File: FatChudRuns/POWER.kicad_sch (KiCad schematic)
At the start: 0 parts

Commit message: add usb c power circuitry, added led for power indication, increased resistance of ethernet leds light to 220ohms
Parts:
- added C21, C22, C23, C24: 1uF, symbol Device:C_Polarized_US
- added D1, D2: LED, symbol Device:LED
- added J4: USB_C_Receptacle_USB2.0_16P, symbol Connector:USB_C_Receptacle_USB2.0_16P
- added R47, R48: 5.1k, Resistor_SMD:R_0603_1608Metric, symbol Device:R
- added R49: 4.7k, Resistor_SMD:R_0603_1608Metric, symbol Device:R
- added R50, R51: 220, Resistor_SMD:R_0603_1608Metric, symbol Device:R
- added SW3: SW_DIP_x01, symbol Switch:SW_DIP_x01
- added U3: USBLC6-2SC6, Package_TO_SOT_SMD:SOT-23-6, symbol Power_Protection:USBLC6-2SC6
- added U5, U6: ST730M33R, SOT_30M33R_STM:SOT_30M33R_STM, symbol ST730:ST730M33R
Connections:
- new net: D2.2 (A), R51.2
- new net: D1.2 (A), R50.2
- new net: J4.A5 (CC1), R48.1
- new net: J4.A6 (D+), J4.B6 (D+), U3.3 (I/O2)
- new net: J4.A7 (D-), J4.B7 (D-), U3.1 (I/O1)
- new net: J4.B5 (CC2), R47.1
- new net +3.3V: C22.1, R51.1, U6.1 (VOUT)
- new net +3.3VA: C24.1, R50.1, U5.1 (VOUT)
- new net +5V: C21.1, C23.1, J4.A4 (VBUS), J4.A9 (VBUS), J4.B4 (VBUS), J4.B9 (VBUS), R49.1, U3.5 (VBUS), U5.3 (VIN), U6.3 (VIN)
- new net GND: C21.2, C22.2, C23.2, C24.2, D1.1 (K), D2.1 (K), J4.A1 (GND), J4.A12 (GND), J4.B1 (GND), J4.B12 (GND), J4.S1 (SHIELD), R47.2, R48.2, SW3.1, U3.2 (GND), U5.2 (GND), U6.2 (GND)
- new net LDO_EN: R49.2, SW3.2, U5.5 (EN), U6.5 (EN)
- new net USB_D+: U3.4 (I/O2)
- new net USB_D-: U3.6 (I/O1)
- no-connect marks 0 -> 4

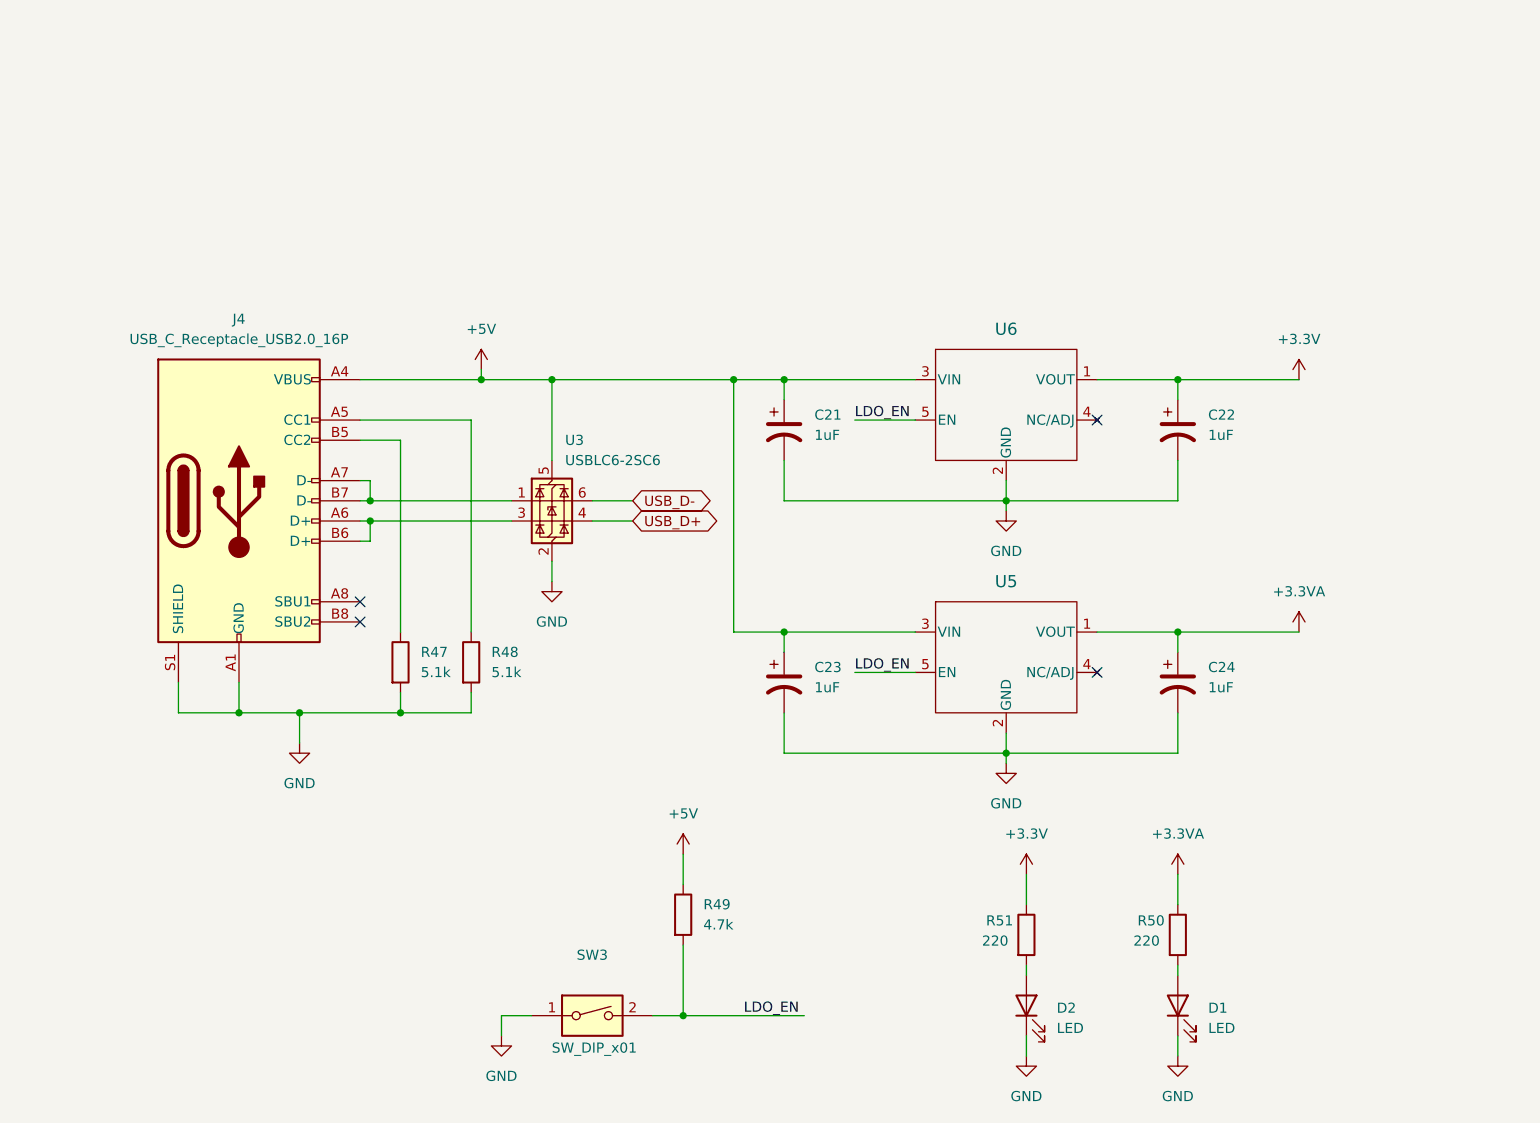
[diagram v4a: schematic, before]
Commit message: sorted out erc errors and warning, connected tvs diodes to jtag
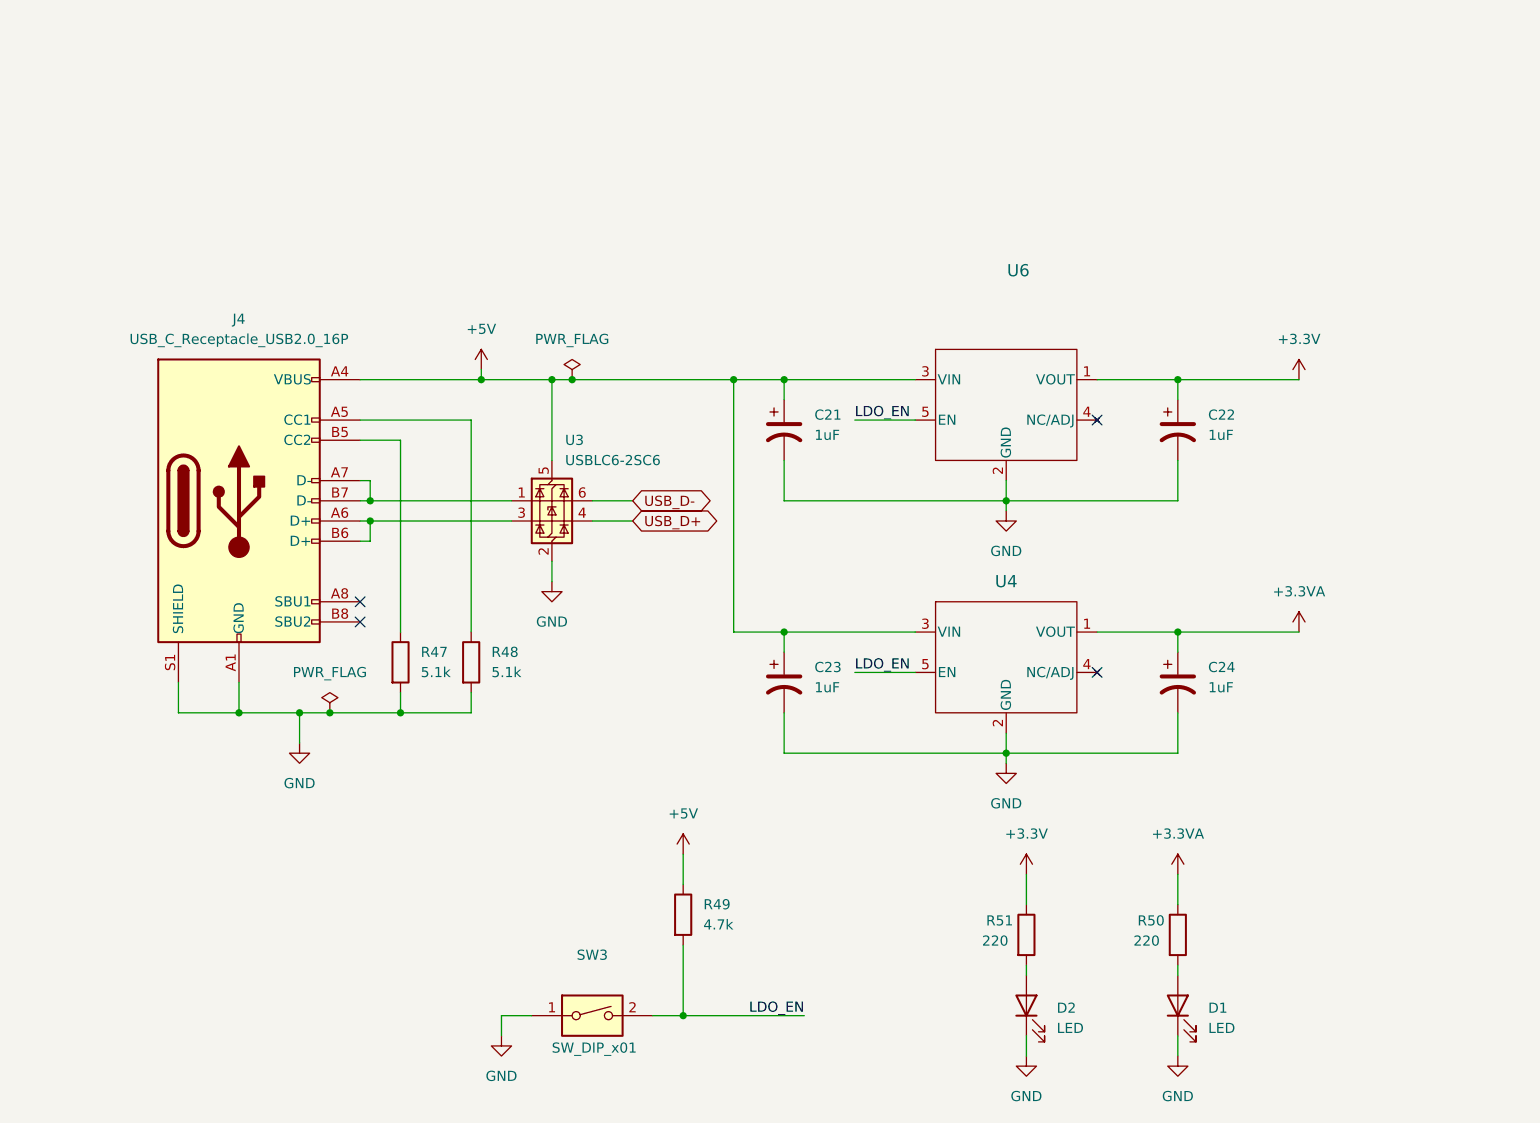
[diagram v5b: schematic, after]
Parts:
- removed U5: ST730M33R, SOT_30M33R_STM:SOT_30M33R_STM, symbol ST730:ST730M33R
- added U4: ST730M33R, SOT_30M33R_STM:SOT_30M33R_STM, symbol ST730:ST730M33R
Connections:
- net +3.3VA: now also U4.1 (VOUT)
- net +5V: now also U4.3 (VIN)
- net GND: now also U4.2 (GND)
- net LDO_EN: now also U4.5 (EN)

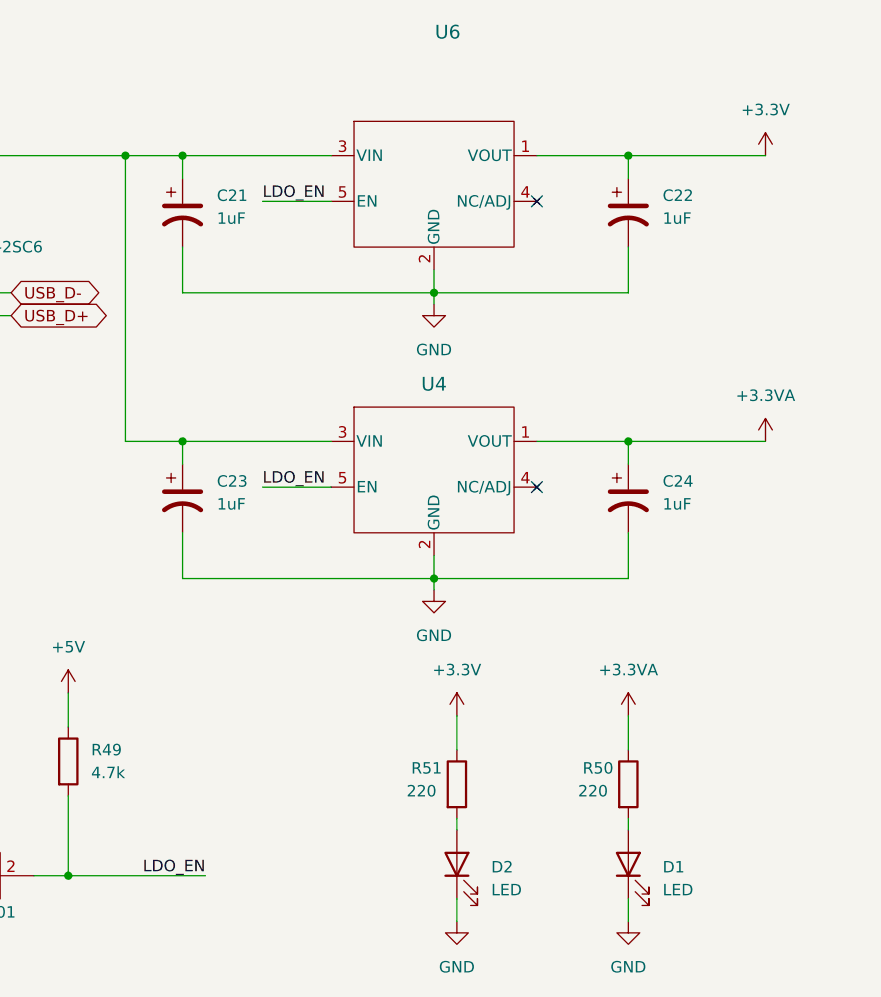
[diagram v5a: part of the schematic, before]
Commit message: added caps and diode footprints, all caps now non-polarized ceramic caps
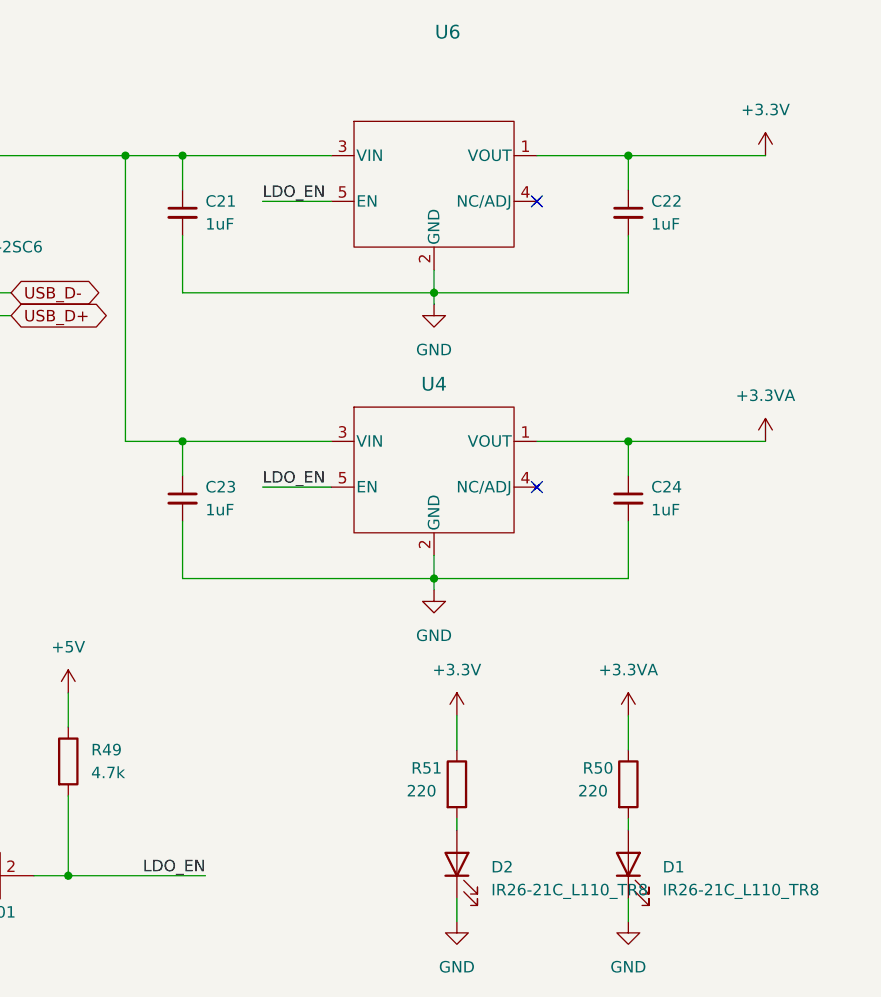
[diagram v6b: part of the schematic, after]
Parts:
- removed C21, C22, C23, C24: 1uF, symbol Device:C_Polarized_US
- removed D1, D2: LED, symbol Device:LED
- added C21, C22, C23, C24: 1uF, Capacitor_SMD:C_0603_1608Metric, symbol Device:C_Small
- added D1, D2: IR26-21C_L110_TR8, LED_SMD:LED_1206_3216Metric, symbol LED:IR26-21C_L110_TR8
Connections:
- net +3.3V: now also C22.1
- net +3.3VA: now also C24.1
- net +5V: now also C21.1, C23.1
- net GND: now also C21.2, C22.2, C23.2, C24.2, D1.1 (K), D2.1 (K)
- net at R51.2: now also D2.2 (A)
- net at R50.2: now also D1.2 (A)

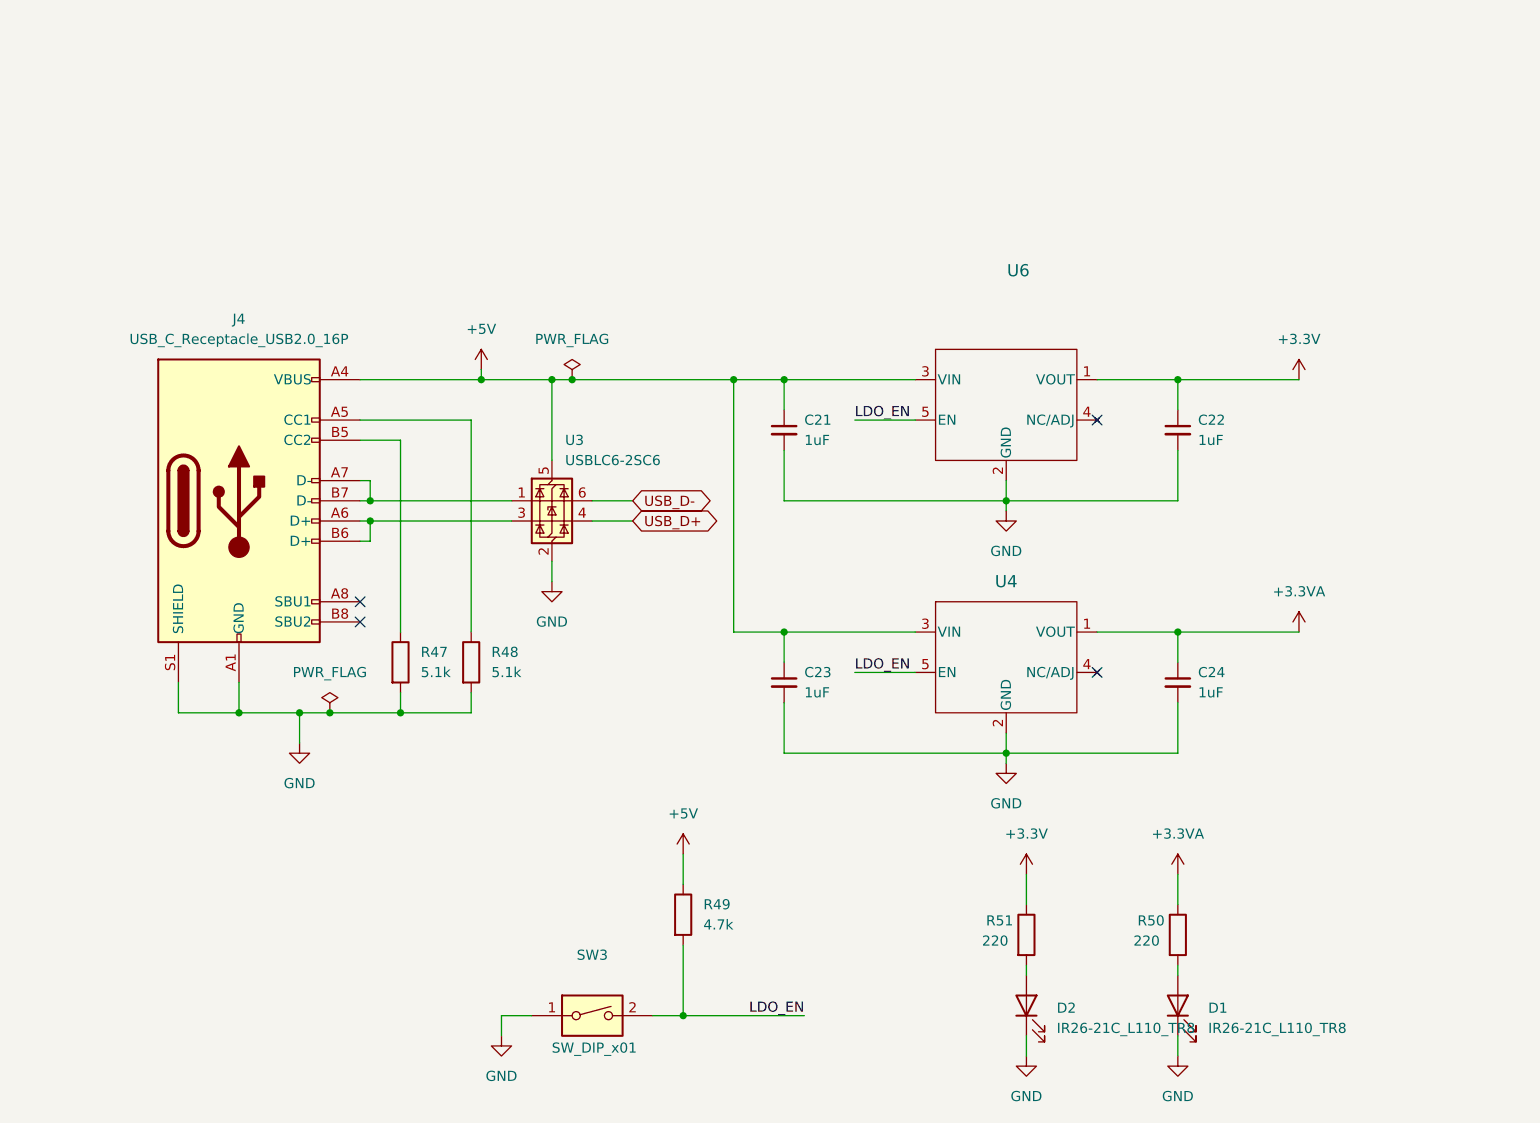
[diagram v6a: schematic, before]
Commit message: added footprint for switches and button - ready for layout
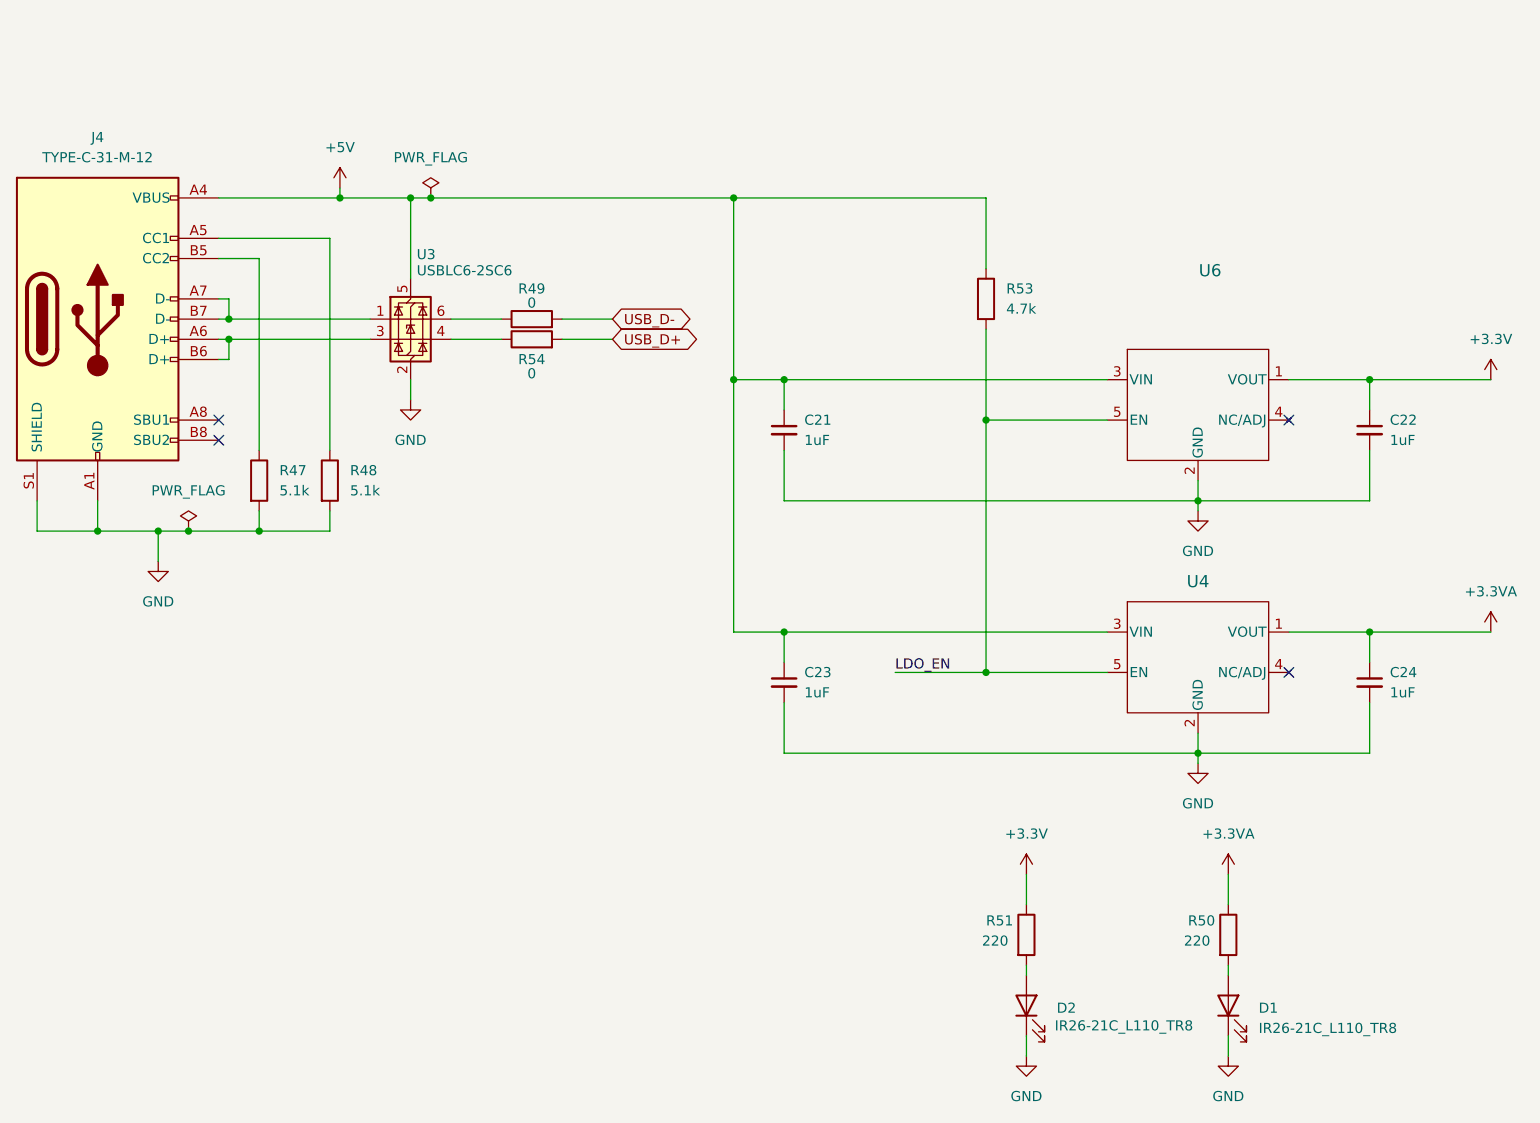
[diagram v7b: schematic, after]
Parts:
- removed SW3: SW_DIP_x01, symbol Switch:SW_DIP_x01
- added R53: 4.7k, Resistor_SMD:R_0603_1608Metric, symbol Device:R
- added R54: 0, Resistor_SMD:R_0603_1608Metric, symbol Device:R
- J4: value USB_C_Receptacle_USB2.0_16P -> TYPE-C-31-M-12; footprint (none) -> Connector_USB:USB_C_Receptacle_GCT_USB4105-xx-A_16P_TopMnt_Horizontal
- R49: value 4.7k -> 0
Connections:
- net +5V: now also R53.1; no longer R49.1
- net LDO_EN: now also R53.2; no longer R49.2
- net USB_D+: now also R54.2; no longer U3.4 (I/O2)
- net USB_D-: now also R49.2; no longer U3.6 (I/O1)
- new net: R49.1, U3.6 (I/O1)
- new net: R54.1, U3.4 (I/O2)
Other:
- moved on the sheet: C22, C24, D1, J4, R47, R48, R50, U3, U4, U6
